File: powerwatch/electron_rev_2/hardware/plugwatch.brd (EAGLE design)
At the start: 73 parts, among them J1 TC2030-JLINK-NL, Q1 MPSA42, T1 DMG3415, U1 MAX-M8, U2 microSD, U3 ISL29035, U37 MPU-9250, U4 NRF51822QF, U5 SAFFB1G56KB0F0A, U6 BGA725L6-ALT, U7 OPA322AIDBVT, X3 16MHz, X4 ABS05-32.768KHZ-9-T

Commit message: Added part numbers and notes
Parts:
- C18, C4: value 0.1uF -> 100nF

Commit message: Schematic almost ready
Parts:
- removed Q1: MPSA42, SparkFun-DiscreteSemi:SOT23-3
- removed U$3: SIP32510, chips:TSOT23-6
- removed U$5: CMB-6544PF, microphone:CMB-6544PF
- removed U2: microSD, SparkFun:MICRO-SD-SOCKET-PP
- added A4: WRL-13678, chips:WRL-13678
- added C12, C13: 100nF, passives:0402_CAP
- added C15: 330pF, passives:0402_CAP
- added J2: DM3AT-SF-PEJM5, connector:DM3AT-SF-PEJM5
- added MK1: AOM-4546P-R, microphones:MIC_AOM-4546P-R
- added S1: PTS645SM43SMTR92, switches:PTS645
- added SW7: SIP3240X, signpost:TDFN4
- added U8: MAX740XESA, chips:SOIC-8
- C10: value 1uf -> 2.2uF; device passives:0402_CAP -> passives:1206
- C6: device passives:0402_CAP -> passives:1206
- C7: value 16pF -> 4.4pF; device passives:0402_CAP -> passives:0603_CAP
- C8: value 25uF -> 10uF; device passives:0402_CAP -> passives:1206
- L2, L3: value (none) -> 1k
- R1: value 1K -> 1k
- R10, R11, R3, R5: value 10K -> 10k
- R16: value 13.7K -> 3.48k; device passives:0402_RES -> passives:0603-RES
- R17, R18, R19: value 100K -> 100k; device passives:0402_RES -> passives:0603-RES
- R2: value 1K -> 10k
- R20: device passives:0402_RES -> passives:0603-RES
- R21: value 75K -> 270k; device passives:0402_RES -> passives:0603-RES
- R4: value 1M -> 10k
- R6, R7: value 10K -> 100k
- R8: value 10K -> 150
- U7: device OPA322AIDBVT:SOT95P280X145-5N -> opamps:SOT23-5
- moved R2 196.2 mm to (-36.7, -266.0)
- moved R4 149.8 mm to (-32.5, -266.0)
- moved R5 148.1 mm to (-28.2, -266.0)
- moved R8 133.1 mm to (-37.1, -280.1)
- moved R7 129.4 mm to (-35.7, -269.7)
- moved C2 119.5 mm to (-21.3, -266.0)
- moved R6 117.3 mm to (-20.6, -260.4)
- moved C10 25.2 mm to (-28.6, -225.4)
- moved U7 24.1 mm to (-14.0, -225.1)
- moved C8 23.6 mm to (-18.6, -225.4)
- moved C6 23.5 mm to (-23.6, -225.4)
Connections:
- net GPS_!RESET renamed !GPS_RESET
- net IMU_SCL renamed SENSORS_SCL
- net IMU_SDA renamed SENSORS_SDA
- removed net N$3: C2.1, R5.2, R6.2, R7.2, R8.2, U$3.1, U$3.2, U2.4
- removed net N$37: Q1.1, R2.2
- removed net NRF_VCC: C18.1, C20.1, J1.1, R13.1, U4.1, U4.12
- removed net SD_DET: R8.1, U2.CD1
- removed net SD_EN: R4.1, U$3.3
- removed net SD_SCK: U2.5
- removed net SD_SS: R5.1, U2.2
- removed net TIMEPULSE: R2.1, U1.4
- new net !SAFEMODE: R8.2, S1.3, S1.4
- new net !SD_CS: J2.2, R4.1
- new net !SD_DETECT: J2.A, R6.1
- new net !WIFI_RESET: A4.6
- new net AUDIO_OUT: U8.5
- new net N$11: C13.1, U8.1, U8.6
- new net N$18: C2.1, J2.4, R2.2, R4.2, R5.2, R6.2, SW7.1
- new net N$6: C15.2, U8.8
- new net SD_ENABLE_POWER: R7.1, SW7.4
- new net SD_SCLK: J2.5
- new net WIFI_RXD: A4.7
- new net WIFI_TXD: A4.2
- net A_MIC_OUT: now also C10.1, U8.2; no longer C10.2
- net GND: now also A4.1, C12.2, C13.2, C15.1, C6.1, J2.6, J2.B, J2.MOUNT0, J2.MOUNT1, J2.MOUNT2, J2.MOUNT3, MK1.TERM-, S1.1, S1.2, SW7.2, SW7.PAD, U8.3; no longer C6.2, Q1.2, U$3.4, U$5.P$5, U2.6, U2.CD2, U2.GND1, U2.GND2
- net N$2: now also U1.4; no longer Q1.3
- net N$4: now also MK1.TERM+; no longer U$5.P$4
- net N$7: now also C10.2; no longer C10.1
- net N$9: now also C6.2; no longer C6.1
- net SD_MISO: now also J2.7, R5.1; no longer R7.1, U2.7
- net SD_MOSI: now also J2.3, R2.1; no longer R6.1, U2.3
- net VCC: now also A4.4, A4.8, C18.1, C20.1, J1.1, R13.1, R7.2, R8.1, SW7.3, U4.1, U4.12; no longer R4.2, U$3.5, U$3.6
- net VCC_A_MIC: now also C12.1, U8.4, U8.7
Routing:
- net NRF_VCC: track 22.9 -> 0.00 mm, vias 3 -> 0
- net VCC: track 0.00 -> 20.0 mm, vias 0 -> 3

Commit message: Schematic done?
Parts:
- removed D3: BLUE, SparkFun-LED:LED-0603
- added D2: LED0603, leds:LED-0603
- added R22: 10k, passives:0402_RES
- added T2: DMG3415, zetex:SOT-23
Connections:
- removed net 3V3: A1.3V3
- removed net IMU_INT: R15.1, U37.12
- new net !IMU_INT: A1.D0, R15.1, U37.12
- new net AUDIO_PWR_EN: A1.B0, R22.1, T2.3
- net !GPS_RESET: now also A1.D4
- net !LIGHT_INT: now also A1.D1
- net !SAFEMODE: now also A1.D7
- net !SD_CS: now also A1.A2
- net !SD_DETECT: now also A1.D6
- net !WIFI_RESET: now also A1.D5
- net AUDIO_OUT: now also A1.B2
- net BLE_RXD: now also A1.C1
- net BLE_TXD: now also A1.C0
- net GPS_PWR_EN: now also A1.D3
- net GPS_RXD: now also A1.TX
- net GPS_TXD: now also A1.RX
- net N$25: now also D2.A; no longer D3.A
- net NRF_P29: now also D2.C; no longer D3.C
- net NRF_SWDIO/!RESET: now also A1.D2
- net SD_MISO: now also A1.A4
- net SD_MOSI: now also A1.A5
- net SD_SCLK: now also A1.A3
- net SENSORS_SCL: now also A1.C5
- net SENSORS_SDA: now also A1.C4
- net VCC: now also A1.3V3, R22.2, T2.2
- net VCC_A_MIC: now also T2.1
- net WIFI_RXD: now also A1.C3
- net WIFI_TXD: now also A1.C2
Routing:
- net N$25: track 1.16 -> 0.00 mm
- net NRF_P29: track 5.07 -> 4.17 mm

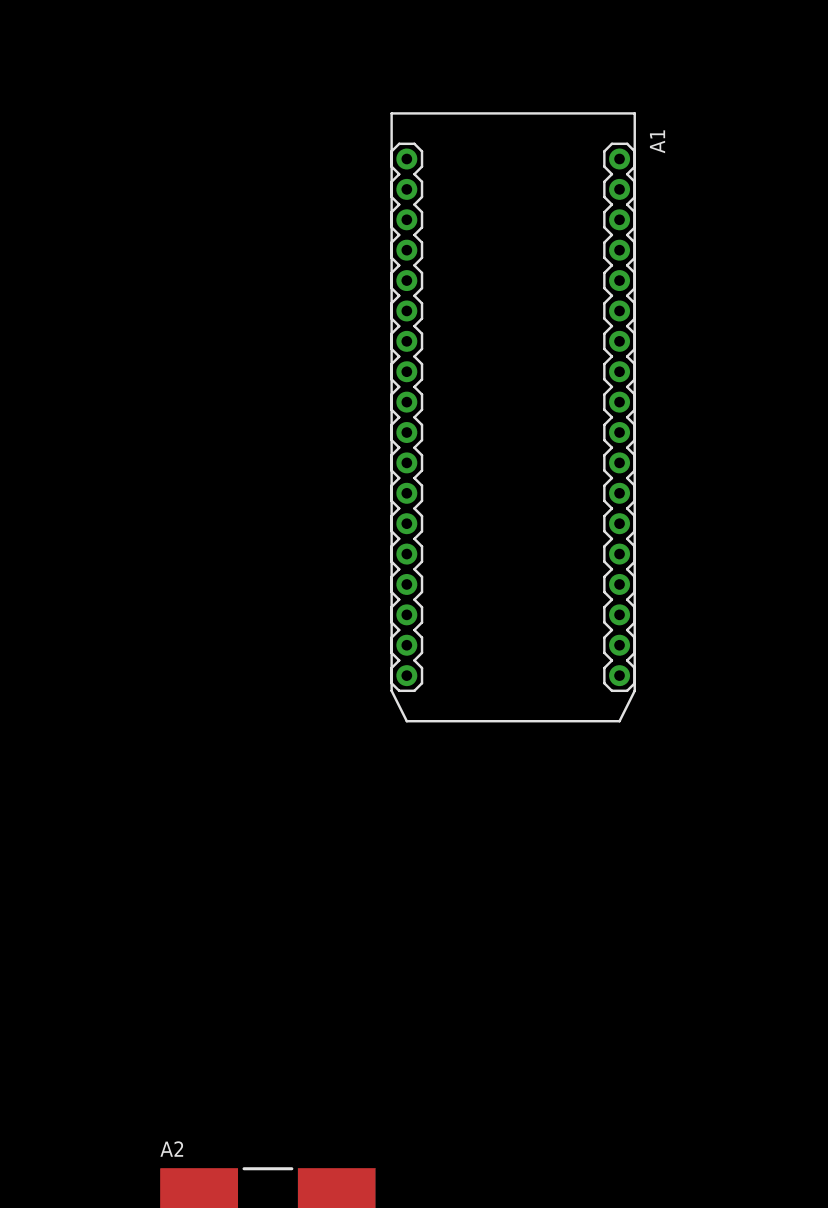
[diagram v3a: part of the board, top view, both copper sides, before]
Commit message: added board outline and annotations
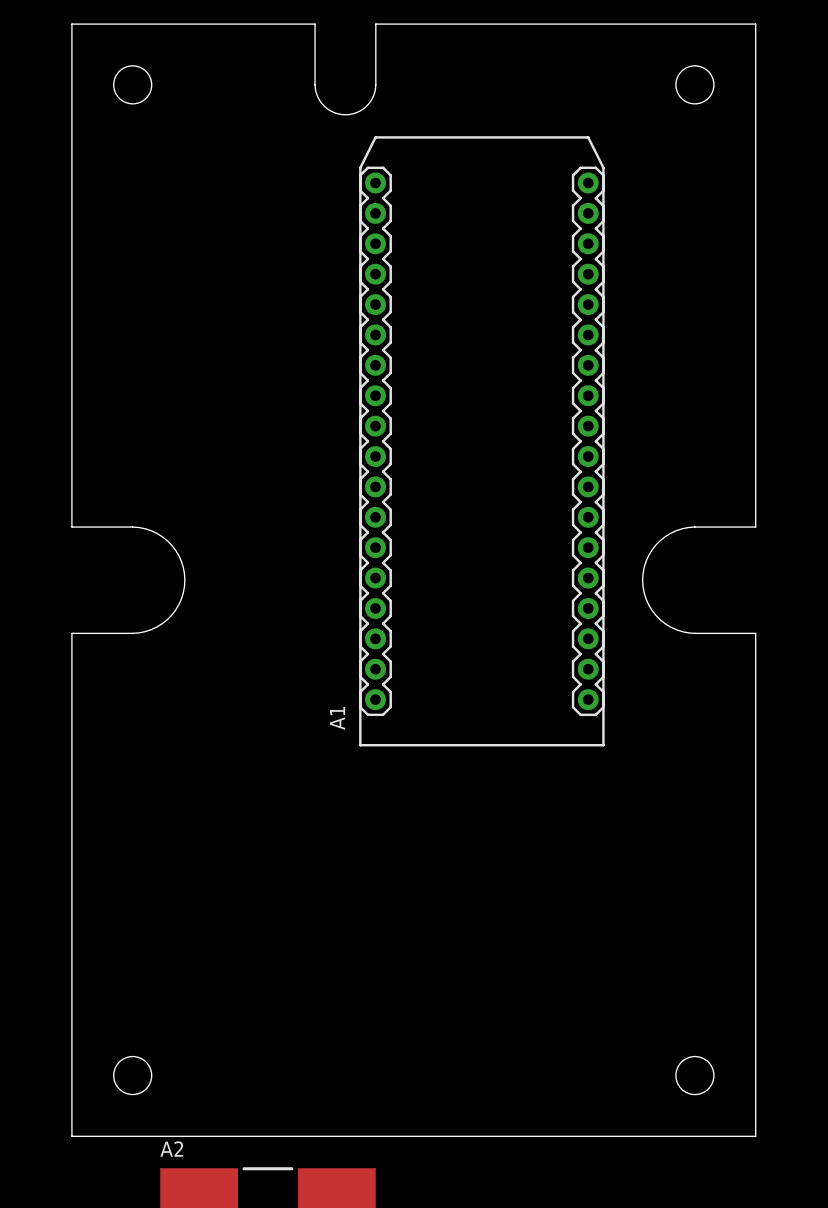
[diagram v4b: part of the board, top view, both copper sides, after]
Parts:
- moved A1 55.7 mm to (44.4, 32.7), turned to 90 degrees
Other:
- board outline added: 57.1 x 93 mm
- board text added: "Antenna Entry (from below)"
- board text added: "Cell Antenna below (No solid groundplane)"
- board text added: "Light Sensor Location (rough, on bottom)"
- board text added: "Mic Location (rough, on bottom)"
- board text added: "Wire Entry (above board)"

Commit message: locked key parts on board, added LED
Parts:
- added D3: LED0603, leds:LED-0603
- added R23: 1k, passives:0402_RES
- moved S1 311.2 mm to (52.1, 12.7), flipped to the bottom
- moved MK1 251.9 mm to (52.1, 22.2), flipped to the bottom
- moved U3 201.6 mm to (52.1, 34.9), flipped to the bottom
- moved A2 36.3 mm to (36.5, 18.5), flipped to the bottom
- moved U37 27.4 mm to (-17.7, -191.1)
- moved A1 6.76 mm to (43.1, 39.3)
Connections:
- new net LED: A1.A1, D3.C
- new net N$3: D3.A, R23.2
- net VCC: now also R23.1
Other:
- outline, holes or cut-outs redrawn
- board text removed: "Light Sensor Location (rough, on bottom)"
- board text removed: "Mic Location (rough, on bottom)"

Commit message: Nothing to do!
Still need to review DRC, clean up signals, and add testpoints.
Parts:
- removed C732: 100nF, passives:0402_CAP
- removed R22: 10k, passives:0402_RES
- removed T1, T2: DMG3415, zetex:SOT-23
- added C30: 100nF, passives:0402_CAP
- added R24, R25, R26: 100k, passives:0402_RES
- added SW1, SW2, SW3, SW4: SIP3240X, signpost:TDFN4
- R3: value 10k -> 100k
- moved R23 369.1 mm to (15.0, 54.1)
- moved D2 320.9 mm to (17.7, 17.4), flipped to the bottom
- moved R7 316.5 mm to (12.8, 43.1), turned to 270 degrees
- moved R2 310.3 mm to (8.64, 40.9), turned to 90 degrees
- moved R4 309.8 mm to (9.91, 40.9), turned to 90 degrees
- moved R5 307.8 mm to (3.30, 40.1), turned to 180 degrees
- moved SW7 307.7 mm to (10.8, 43.1), turned to 270 degrees
- moved C2 307.4 mm to (5.84, 40.1), turned to 180 degrees
- moved R8 303.2 mm to (55.6, 8.56), flipped to the bottom, turned to 180 degrees
- moved R6 301.3 mm to (1.52, 40.1), turned to 90 degrees
- moved C15 287.4 mm to (49.8, 38.1), turned to 270 degrees
- moved C13 280.7 mm to (42.2, 36.6), turned to 90 degrees
- moved J2 280.0 mm to (8.00, 38.1)
- moved C12 272.9 mm to (42.9, 31.0), turned to 180 degrees
- moved U8 269.8 mm to (47.0, 34.3), turned to 270 degrees
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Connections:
- new net BLE_PWR_EN: A1.B5, R24.1, SW4.4
- new net BLE_VCC: R13.1
- new net N$14: A4.4, A4.8, SW3.1
- new net VCC_BLE: C18.1, C20.1, J1.1, SW4.1, U4.1, U4.12
- new net WIFI_PWR_EN: A1.A0, R26.1, SW3.4
- net AUDIO_PWR_EN: now also R25.1, SW2.4; no longer R22.1, T2.3
- net GND: now also C30.2, SW1.2, SW1.PAD, SW2.2, SW2.PAD, SW3.2, SW3.PAD, SW4.2, SW4.PAD; no longer C732.2
- net GPS_PWR_EN: now also SW1.4; no longer T1.3
- net GPS_VCC: now also SW1.1; no longer T1.1, U1.6
- net VCC: now also C30.1, R24.2, R25.2, R26.2, SW1.3, SW2.3, SW3.3, SW4.3; no longer A4.4, A4.8, C18.1, C20.1, C732.1, J1.1, R13.1, R22.2, T1.2, T2.2, U4.1, U4.12
- net VCC_A_MIC: now also SW2.1; no longer T2.1
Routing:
- net BLE_TXD: track 0.00 -> 95.9 mm, vias 0 -> 1
- net BLE_RXD: track 0.00 -> 87.2 mm, vias 0 -> 2
- net BLE_PWR_EN: track 0.00 -> 86.9 mm, vias 0 -> 1
- net !SAFEMODE: track 0.00 -> 75.5 mm, vias 0 -> 1
- net SENSORS_SDA: track 0.00 -> 73.2 mm
- net SENSORS_SCL: track 0.00 -> 71.4 mm, vias 0 -> 1
- net NRF_SWDIO/!RESET: track 6.67 -> 75.0 mm, vias 0 -> 2
- net AUDIO_PWR_EN: track 0.00 -> 62.6 mm
- net VCC: track 20.0 -> 74.0 mm, vias 3 -> 12
- net AUDIO_OUT: track 0.00 -> 53.5 mm, vias 0 -> 1
- net SD_MISO: track 0.00 -> 52.4 mm, vias 0 -> 2
- net !WIFI_RESET: track 0.00 -> 52.4 mm
- net !LIGHT_INT: track 0.00 -> 52.0 mm
- net SD_SCLK: track 0.00 -> 51.2 mm, vias 0 -> 2
- net !SD_CS: track 0.00 -> 49.9 mm, vias 0 -> 2
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- added copper zone on layer 2, net GND
- added copper zone on layer 1, net N$33
- added copper zone on layer 15, net N$33
- added copper zone on layer 16, net N$33
- added copper zone on layer 2, net N$33
- added copper zone on layer 16, net N$34
- added copper zone on layer 1, net N$37
- added copper zone on layer 15, net VCC
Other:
- board text removed: "2014/10/08"

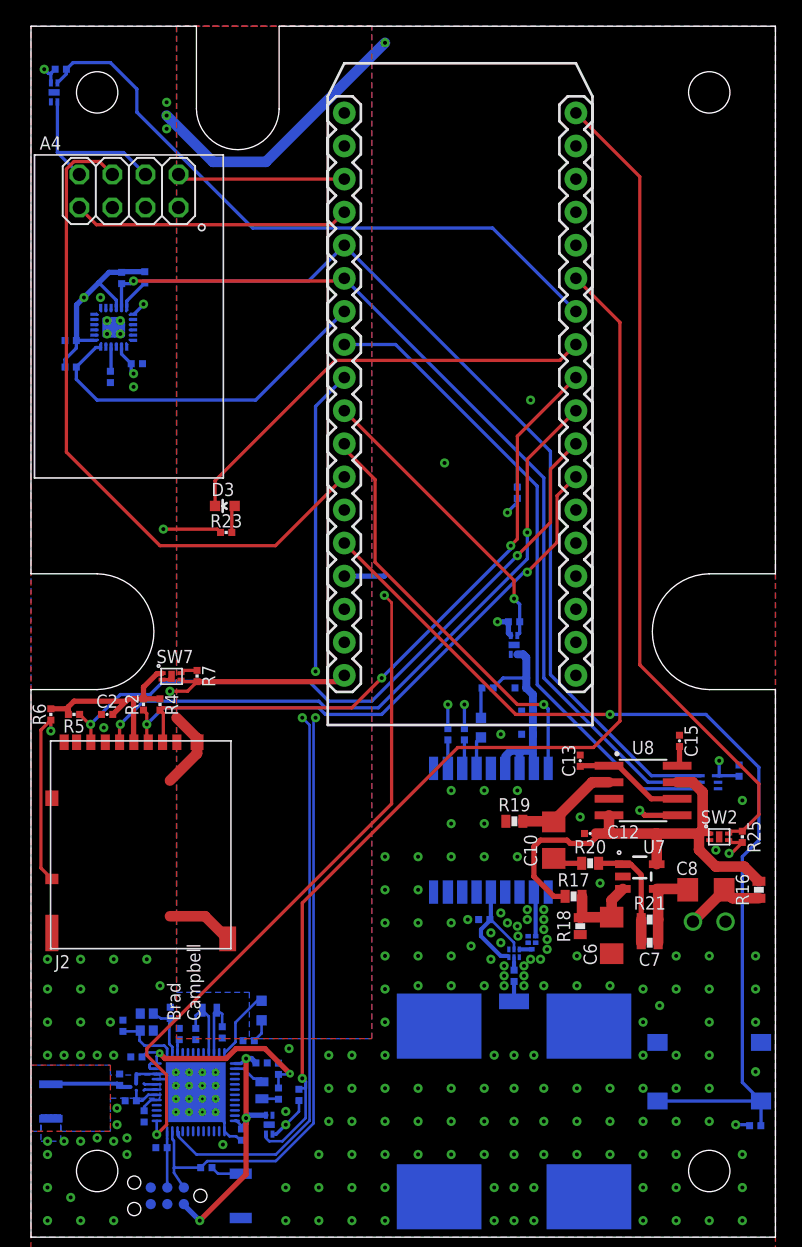
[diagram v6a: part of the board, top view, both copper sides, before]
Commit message: Reroute, move signals on Electron
Add names/dates/revision
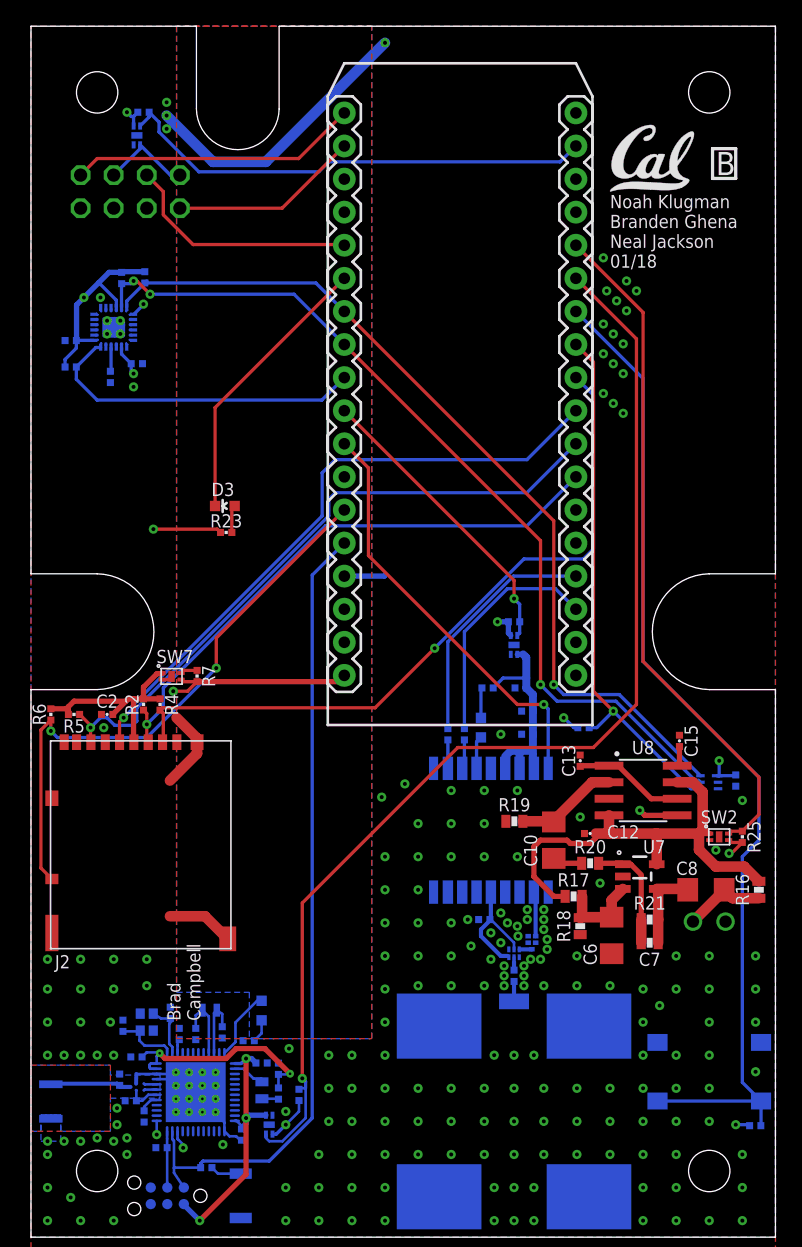
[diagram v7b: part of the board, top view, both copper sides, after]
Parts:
- added U$3: (no value), logos:UCB_CAL_200MIL
- moved R9 18.7 mm to (42.4, 39.1), turned to 0 degrees
- moved R26 7.16 mm to (8.64, 86.4)
- moved SW3 7.16 mm to (8.13, 84.6)
- moved C14 0.80 mm to (54.1, 35.1), turned to 270 degrees
- moved A4 0.11 mm to (7.62, 80.3), flipped to the bottom
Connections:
- net !IMU_INT: now also A1.D2; no longer A1.D0
- net !LIGHT_INT: now also A1.A1; no longer A1.D1
- net !SAFEMODE: now also A1.A0; no longer A1.D7
- net !WIFI_RESET: now also A1.C4; no longer A1.D5
- net AUDIO_PWR_EN: now also A1.B4; no longer A1.B0
- net BLE_RXD: now also A1.C3; no longer A1.C1
- net BLE_TXD: now also A1.C2; no longer A1.C0
- net GPS_VCC: now also U1.6
- net LED: now also A1.C5; no longer A1.A1
- net NRF_SWDIO/!RESET: now also A1.D7; no longer A1.D2
- net SENSORS_SCL: now also A1.D1; no longer A1.C5
- net SENSORS_SDA: now also A1.D0; no longer A1.C4
- net WIFI_PWR_EN: now also A1.B1; no longer A1.A0
- net WIFI_RXD: now also A1.C1; no longer A1.C3
- net WIFI_TXD: now also A1.C0; no longer A1.C2
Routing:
- net !WIFI_RESET: track 52.4 -> 18.4 mm
- net NRF_SWDIO/!RESET: track 75.0 -> 62.2 mm, vias 2 -> 0
- net LED: track 34.0 -> 21.6 mm
- net WIFI_PWR_EN: track 49.6 -> 37.3 mm
- net !LIGHT_INT: track 52.0 -> 40.9 mm, vias 0 -> 1
- net BLE_TXD: track 95.9 -> 85.1 mm
- net AUDIO_PWR_EN: track 62.6 -> 52.5 mm
- net WIFI_TXD: track 12.9 -> 22.2 mm
- net BLE_RXD: track 87.2 -> 78.7 mm, vias 2 -> 1
- net WIFI_RXD: track 21.3 -> 14.6 mm
- net N$14: track 13.7 -> 7.18 mm
- net SENSORS_SDA: track 73.2 -> 68.3 mm, vias 0 -> 1
- net !SD_CS: track 49.9 -> 54.7 mm, vias 2 -> 1
- net GPS_RXD: track 13.4 -> 18.0 mm, vias 1 -> 0
- net GPS_TXD: track 15.8 -> 18.6 mm, vias 1 -> 0
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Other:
- board text added: "B"
- board text added: "Noah Klugman Branden Ghena Neal Jackson 01/18"
